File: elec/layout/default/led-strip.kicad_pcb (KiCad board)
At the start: 2 copper layers, 10.2 x 409.7 mm, 43 parts

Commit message: Change layout to be 10 pixels
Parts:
- removed CLED11, CLED12, CLED13, CLED14, CLED15, CLED16, CLED17, CLED18, CLED19, CLED20: Multilayer Ceramic Capacitors MLCC - SMD/SMT 100nF 10V 0402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, lib:C0402
- removed LED11, LED12, LED13, LED14, LED15, LED16, LED17, LED18, LED19, LED20: , lib:LED-SMD_4P-L5.0-W5.0-TL
- removed R1: Chip Resistor - Surface Mount 100Ohms ±5% 1/8W 0805 RoHS, lib:R0805
- moved U2 208.5 mm to (44.4, 248.7)
- moved CLED10 4.31 mm to (48.4, 245.2)
- moved LED10 4.31 mm to (48.4, 240.3)
- moved CLED9 3.69 mm to (48.4, 225.3)
- moved LED9 3.69 mm to (48.4, 220.4)
- moved LED8 3.07 mm to (48.4, 200.6)
- moved CLED8 3.07 mm to (48.4, 205.5)
- moved LED7 2.45 mm to (48.4, 180.8)
- moved CLED7 2.45 mm to (48.4, 185.7)
- moved CLED3 1.98 mm to (48.4, 104.4)
- moved LED3 1.98 mm to (48.4, 99.5)
- moved CLED6 1.83 mm to (48.4, 165.9)
- moved LED6 1.83 mm to (48.4, 161.0)
- moved CLED2 1.36 mm to (48.4, 84.6)
- moved LED2 1.36 mm to (48.4, 79.7)
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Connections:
- LED10 pad 2: do-9 -> p3-1
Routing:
- net vcc: track 571.8 -> 280.8 mm
- net gnd: track 518.8 -> 259.8 mm
- net p4: track 406.2 -> 197.6 mm
- net do-18: track 19.3 -> 0.00 mm
- net do-9: track 19.3 -> 0.00 mm
- net do-15: track 19.3 -> 0.00 mm
- net do-14: track 19.3 -> 0.00 mm
- net do-13: track 19.3 -> 0.00 mm
- net do-17: track 19.3 -> 0.00 mm
- net do-16: track 19.3 -> 0.00 mm
- net do-12: track 19.3 -> 0.00 mm
- net do-11: track 19.3 -> 0.00 mm
- net do-10: track 19.3 -> 0.00 mm
- net p3-1: track 11.7 -> 8.32 mm
- net do-2: track 19.3 -> 20.7 mm
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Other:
- board size 10.2 x 409.7 mm -> 10.2 x 200 mm

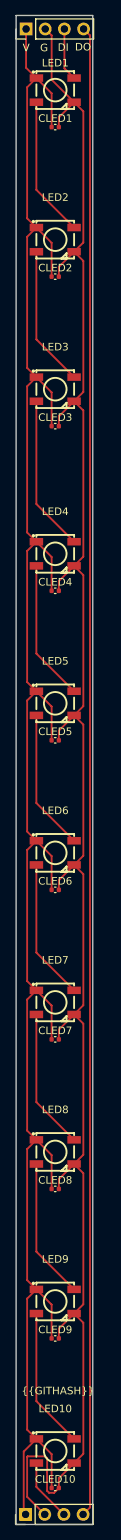
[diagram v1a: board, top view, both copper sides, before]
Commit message: change to 12 LED's per 20cm
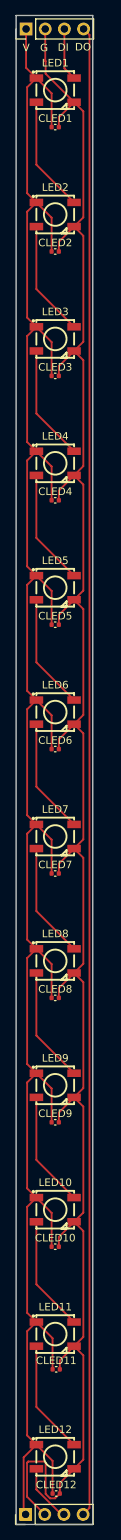
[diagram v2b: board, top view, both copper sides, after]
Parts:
- added CLED11: Multilayer Ceramic Capacitors MLCC - SMD/SMT 100nF 10V 0402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, lib:C0402, F.Cu at (48.5, 229.4)
- added CLED12: Multilayer Ceramic Capacitors MLCC - SMD/SMT 100nF 10V 0402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, lib:C0402, F.Cu at (48.5, 245.9)
- added LED11: , lib:LED-SMD_4P-L5.0-W5.0-TL, F.Cu at (48.4, 224.8)
- added LED12: , lib:LED-SMD_4P-L5.0-W5.0-TL, F.Cu at (48.4, 241.0)
- moved LED10 32.0 mm to (48.4, 208.3)
- moved CLED10 32.0 mm to (48.4, 213.2)
- moved CLED9 28.6 mm to (48.4, 196.7)
- moved LED9 28.6 mm to (48.4, 191.8)
- moved CLED8 25.3 mm to (48.4, 180.2)
- moved LED8 25.3 mm to (48.4, 175.3)
- moved CLED7 22.0 mm to (48.4, 163.7)
- moved LED7 22.0 mm to (48.4, 158.8)
- moved CLED6 18.7 mm to (48.4, 147.2)
- moved LED6 18.7 mm to (48.4, 142.3)
- moved LED5 15.3 mm to (48.4, 125.8)
- moved CLED5 15.3 mm to (48.4, 130.7)
- moved CLED4 12.0 mm to (48.4, 114.3)
- moved LED4 12.0 mm to (48.4, 109.4)
- moved CLED3 6.66 mm to (48.4, 97.8)
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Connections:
- LED10 pad 2: p3-1 -> do-9
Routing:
- net vcc: track 280.8 -> 297.3 mm
- net do-9: track 0.00 -> 15.4 mm
- net do-10: track 0.00 -> 15.1 mm
- net gnd: track 259.8 -> 269.9 mm
- net do-2: track 20.7 -> 15.4 mm
- net do-8: track 18.7 -> 15.4 mm
- net do-5: track 18.7 -> 15.4 mm
- net do-4: track 18.7 -> 15.4 mm
- net do-3: track 18.7 -> 15.4 mm
- net do-7: track 18.7 -> 15.4 mm
- net do-6: track 18.7 -> 15.4 mm
- net do: track 18.7 -> 15.4 mm
- net do-1: track 18.7 -> 15.4 mm
- net p3-1: track 8.32 -> 7.76 mm
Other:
- board text removed: "{{GITHASH}}"
